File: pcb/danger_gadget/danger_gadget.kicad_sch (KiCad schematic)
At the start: 5 parts, among them J1 Conn_01x02_Pin, Q1 MTA100N10KRI3

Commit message: update curcuit
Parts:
- removed D1: 1N4007, Diode_THT:D_DO-41_SOD81_P10.16mm_Horizontal, symbol Diode:1N4007
- added BZ1: Buzzer, symbol Device:Buzzer
- added D1, D3, D4: LED_Small, symbol Device:LED_Small
- added D2: 1N4007, symbol Device:D_Small
- added J2, J3: Conn_01x05_Pin, symbol Connector:Conn_01x05_Pin
- added R3, R4: 10k, symbol Device:R_Small
- added R5, R6, R7: 330, symbol Device:R_Small
- added R8, R9: 220k, symbol Device:R_Small
- added SW1: SW_Rotary_1x6_MP, symbol Switch:SW_Rotary_1x6_MP
- added SW2: SW_DIP_x05, symbol Switch:SW_DIP_x05
- added SW3, SW4, SW5: SW_Push, symbol Switch:SW_Push
- added U1: ESP32-WROOM-32E, RF_Module:ESP32-WROOM-32D, symbol RF_Module:ESP32-WROOM-32E
- added U2: MCP23017x-x-SP, Package_DIP:DIP-28_W7.62mm, symbol Interface_Expansion:MCP23017x-x-SP
- R1: value R_Small -> 1k
- R2: value R_Small -> 10k
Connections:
- net +5V: now also D2.1 (K)
- net GND: now also BZ1.2 (-), D1.1 (K), D3.1 (K), D4.1 (K), J3.1 (Pin_1), J3.2 (Pin_2), J3.3 (Pin_3), J3.4 (Pin_4), J3.5 (Pin_5), SW1.7, SW2.10, SW2.6, SW2.7, SW2.8, SW2.9, SW3.2, SW4.2, SW5.2, U1.1 (GND), U1.15 (GND), U1.38 (GND), U1.39 (GND), U2.10 (V_{SS}), U2.15 (A0), U2.16 (A1), U2.17 (A2)
- net at J1.2 (Pin_2), Q1.D: now also D2.2 (A)
- net Solenoid Out: now reaches R1.1
- net Solenoid Out: now also U1.37 (IO23)
- new net: SW2.1, U2.21 (GPA0)
- new net: SW2.2, U2.22 (GPA1)
- new net: SW2.3, U2.23 (GPA2)
- new net: SW2.4, U2.24 (GPA3)
- new net: SW2.5, U2.25 (GPA4)
- new net: SW1.1, U2.3 (GPB2)
- new net: SW1.2, U2.4 (GPB3)
- new net: SW1.3, U2.5 (GPB4)
- new net: SW1.4, U2.6 (GPB5)
- new net: SW1.5, U2.7 (GPB6)
- new net: SW1.6, U2.8 (GPB7)
- new net: D4.2 (A), R7.2
- new net: D3.2 (A), R6.2
- new net: D1.2 (A), R5.2
- new net: J2.4 (Pin_4), U2.1 (GPB0)
- new net: J2.5 (Pin_5), U2.2 (GPB1)
- new net: J2.1 (Pin_1), U2.26 (GPA5)
- new net: J2.2 (Pin_2), U2.27 (GPA6)
- new net: J2.3 (Pin_3), U2.28 (GPA7)
- new net +3V3: R3.1, R4.1, U1.2 (VDD), U2.18 (~{RESET}), U2.9 (V_{DD})
- new net +BATT: R8.2
- new net -BATT: R9.1
- new net Battery ADC: R8.1, R9.2, U1.16 (IO13)
- new net Buzzer Out: BZ1.1 (+), U1.30 (IO18)
- new net ExIO Interrupt: U1.31 (IO19), U2.20 (INTA)
- new net I2C SCL: R4.2, U1.36 (IO22), U2.12 (SCK)
- new net I2C SDA: R3.2, U1.33 (IO21), U2.13 (SDA)
- new net LED A: R5.1, U1.8 (IO32)
- new net LED B: R6.1, U1.9 (IO33)
- new net LED C: R7.1, U1.10 (IO25)
- new net Push A: SW3.1, U1.11 (IO26)
- new net Push B: SW4.1, U1.12 (IO27)
- new net Push C: SW5.1, U1.13 (IO14)
- no-connect marks 0 -> 2
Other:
- moved on the sheet: J1, Q1, R1, R2

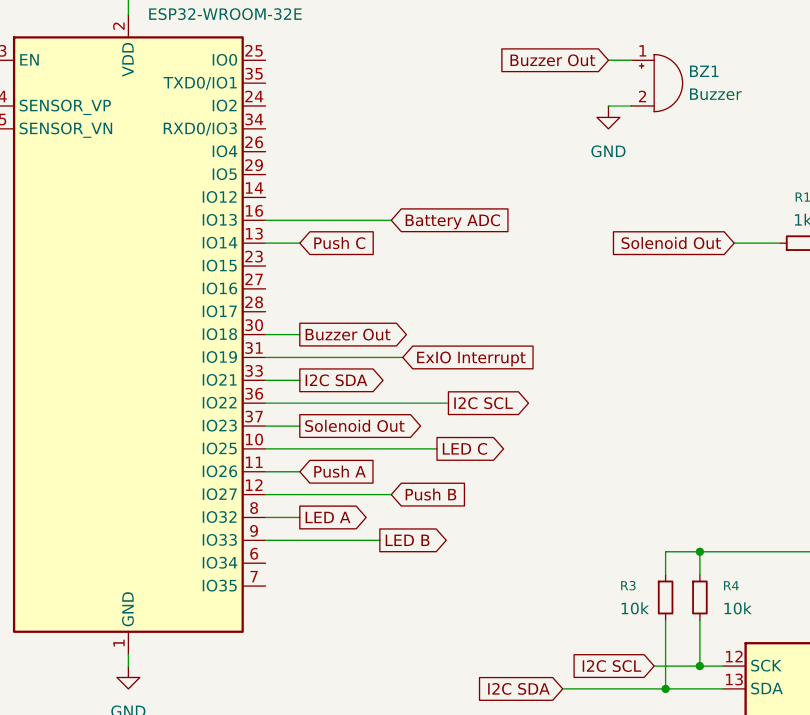
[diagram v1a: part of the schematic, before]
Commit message: fix adc pin
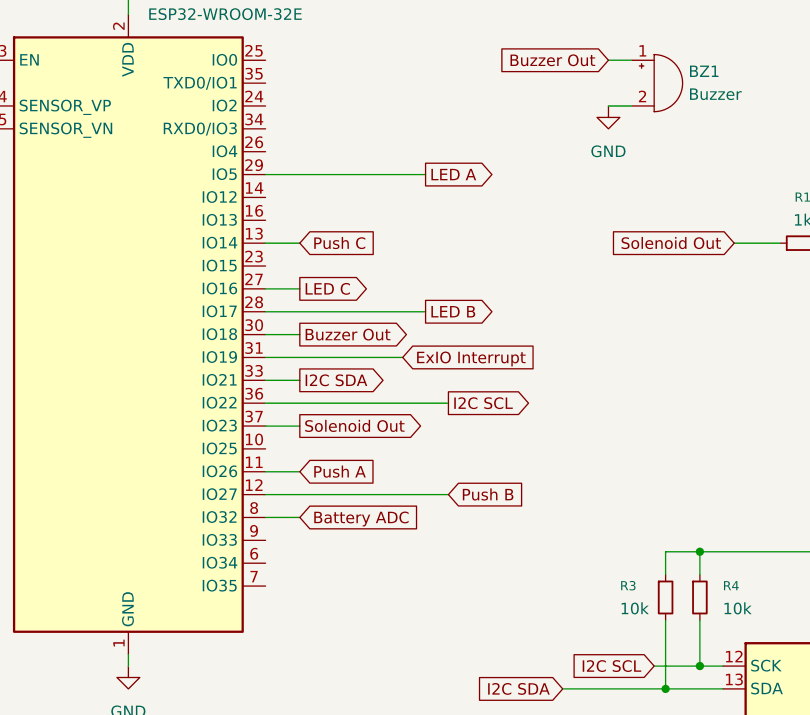
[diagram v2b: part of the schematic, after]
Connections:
- net Battery ADC: now also U1.8 (IO32); no longer U1.16 (IO13)
- net LED A: now also U1.29 (IO5); no longer U1.8 (IO32)
- net LED B: now also U1.28 (IO17); no longer U1.9 (IO33)
- net LED C: now also U1.27 (IO16); no longer U1.10 (IO25)

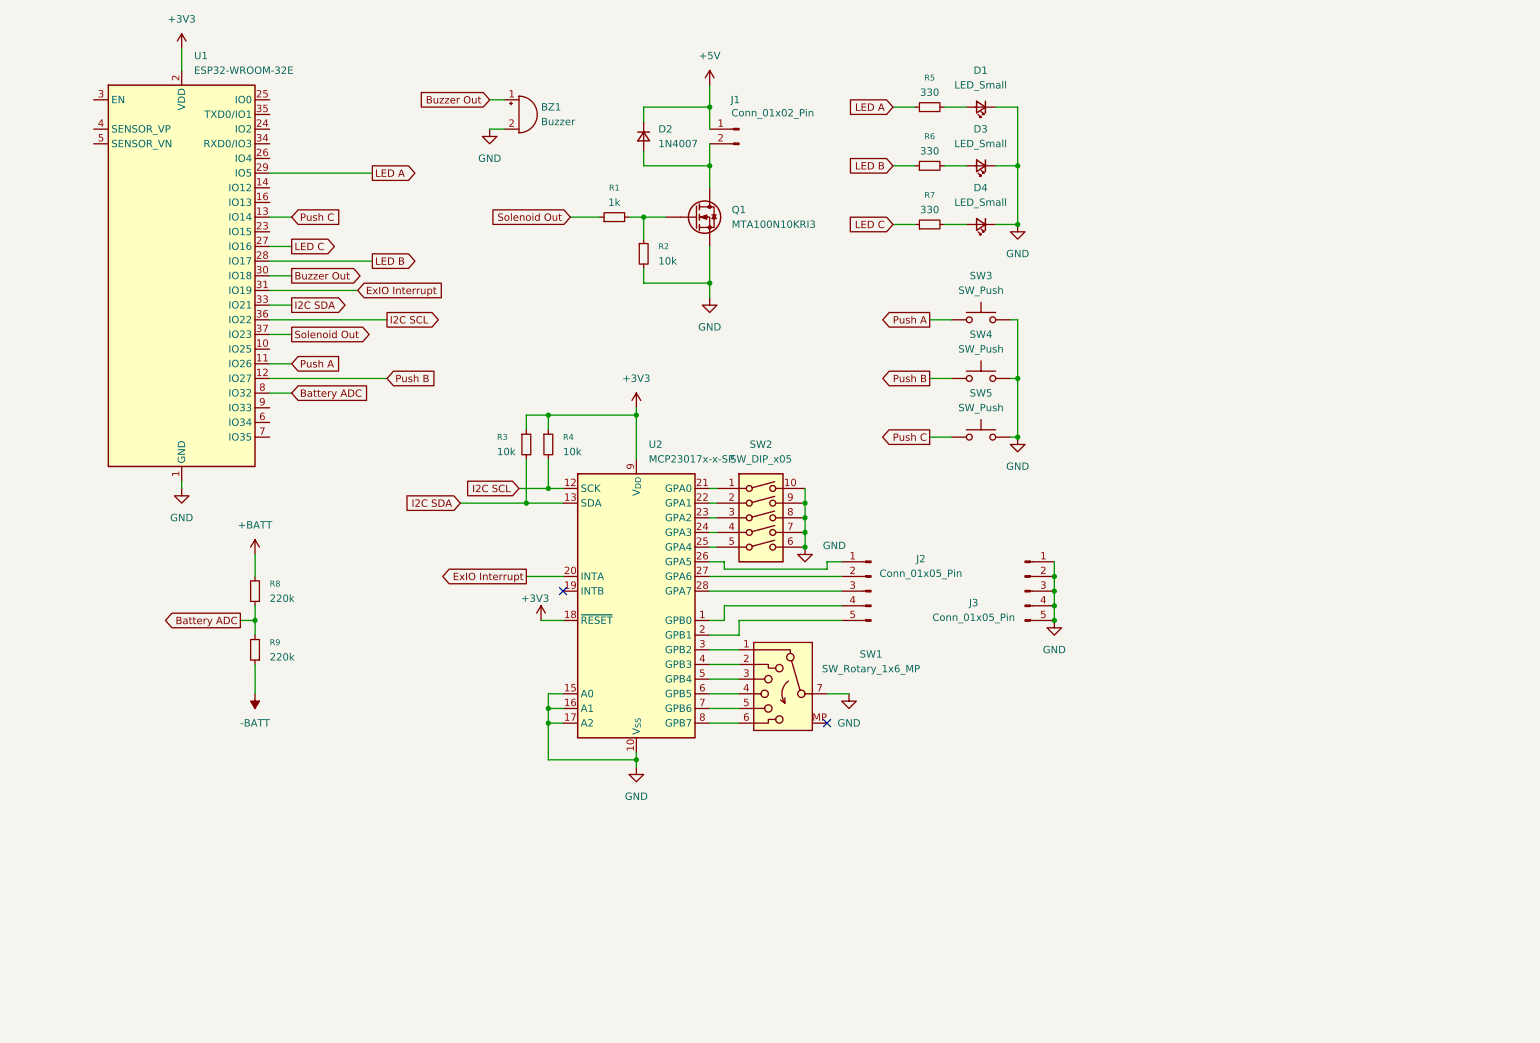
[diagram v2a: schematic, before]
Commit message: fix Danger Gadget Curcuit. add tranceiver_connector kicad file
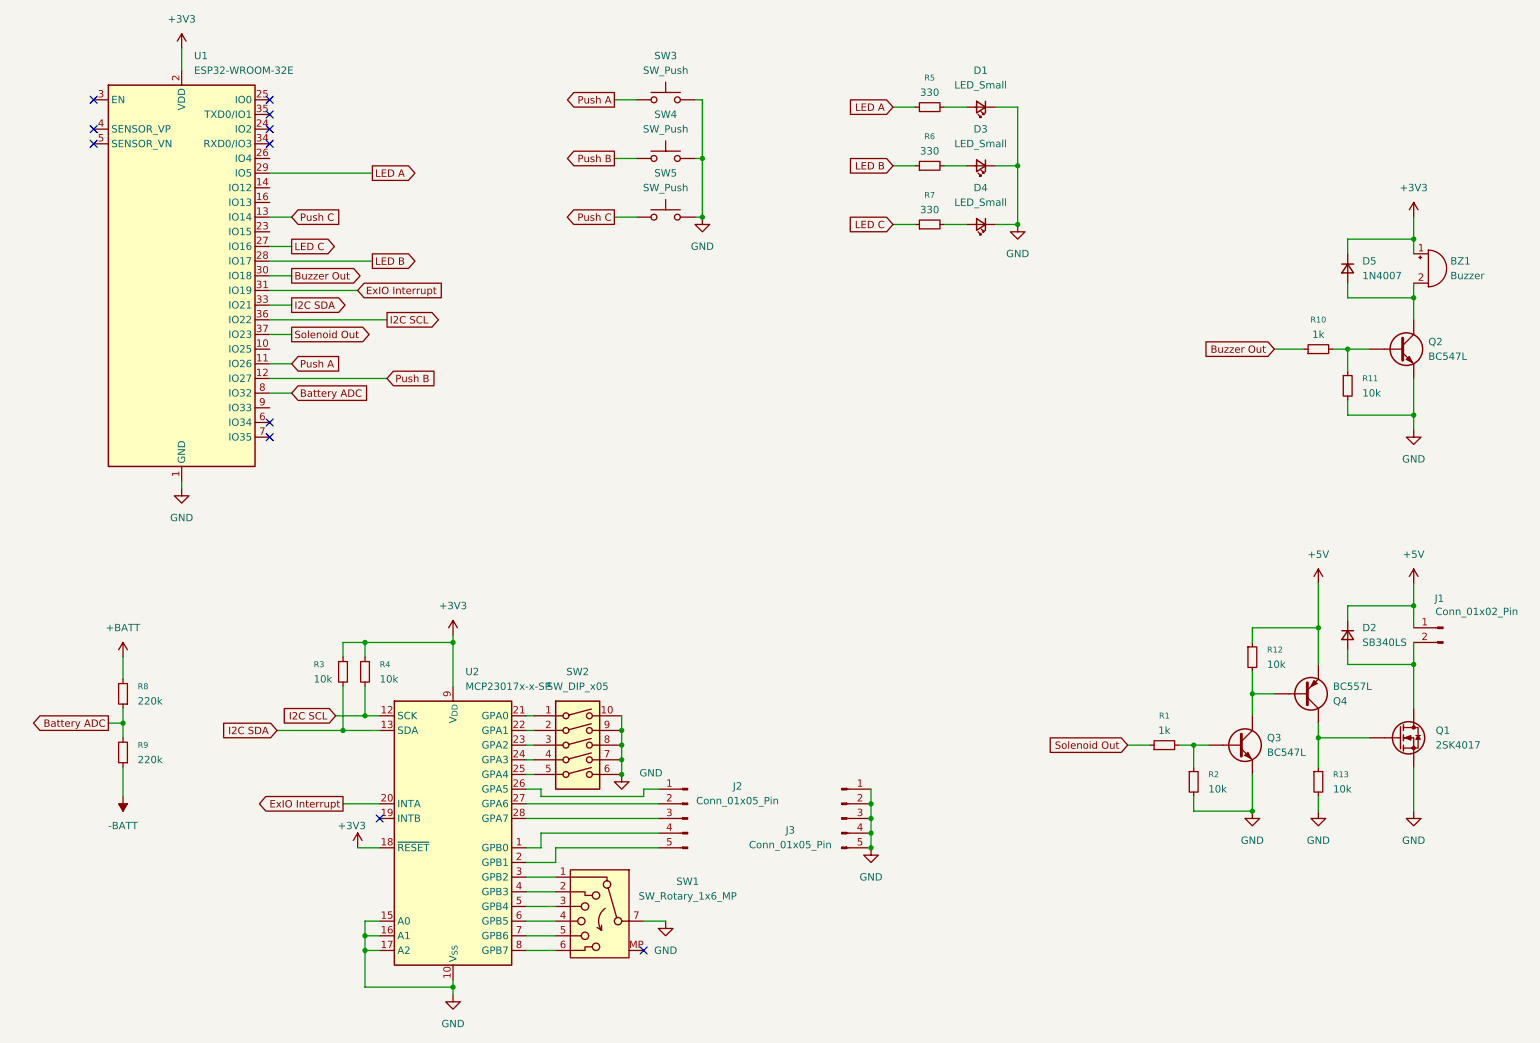
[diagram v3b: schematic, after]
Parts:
- added D5: 1N4007, symbol Device:D_Small
- added Q2, Q3: BC547L, symbol Device:Q_NPN
- added Q4: BC557L, symbol Device:Q_PNP
- added R10: 1k, symbol Device:R_Small
- added R11, R12, R13: 10k, symbol Device:R_Small
- D2: value 1N4007 -> SB340LS
- Q1: value MTA100N10KRI3 -> 2SK4017
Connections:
- net +3V3: now also BZ1.1 (+), D5.1 (K)
- net +5V: now also Q4.E, R12.1
- net Buzzer Out: now also R10.1; no longer BZ1.1 (+)
- net GND: now also Q2.E, Q3.E, R11.2, R13.2; no longer BZ1.2 (-)
- net at R1.2, R2.1: now also Q3.B; no longer Q1.G
- new net: Q2.B, R10.2, R11.1
- new net: BZ1.2 (-), D5.2 (A), Q2.C
- new net: Q1.G, Q4.C, R13.1
- new net: Q3.C, Q4.B, R12.2
- no-connect marks 2 -> 11
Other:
- moved on the sheet: D2, J1, J2, J3, R3, R4, R8, R9, SW1, SW2, SW3, SW4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
